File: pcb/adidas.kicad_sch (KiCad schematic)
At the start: 32 parts, among them J1 ISP Header, J7 Battery, J9 Shitty Add-on, U1 MPU-6050, U2 ATTINY841-SSU

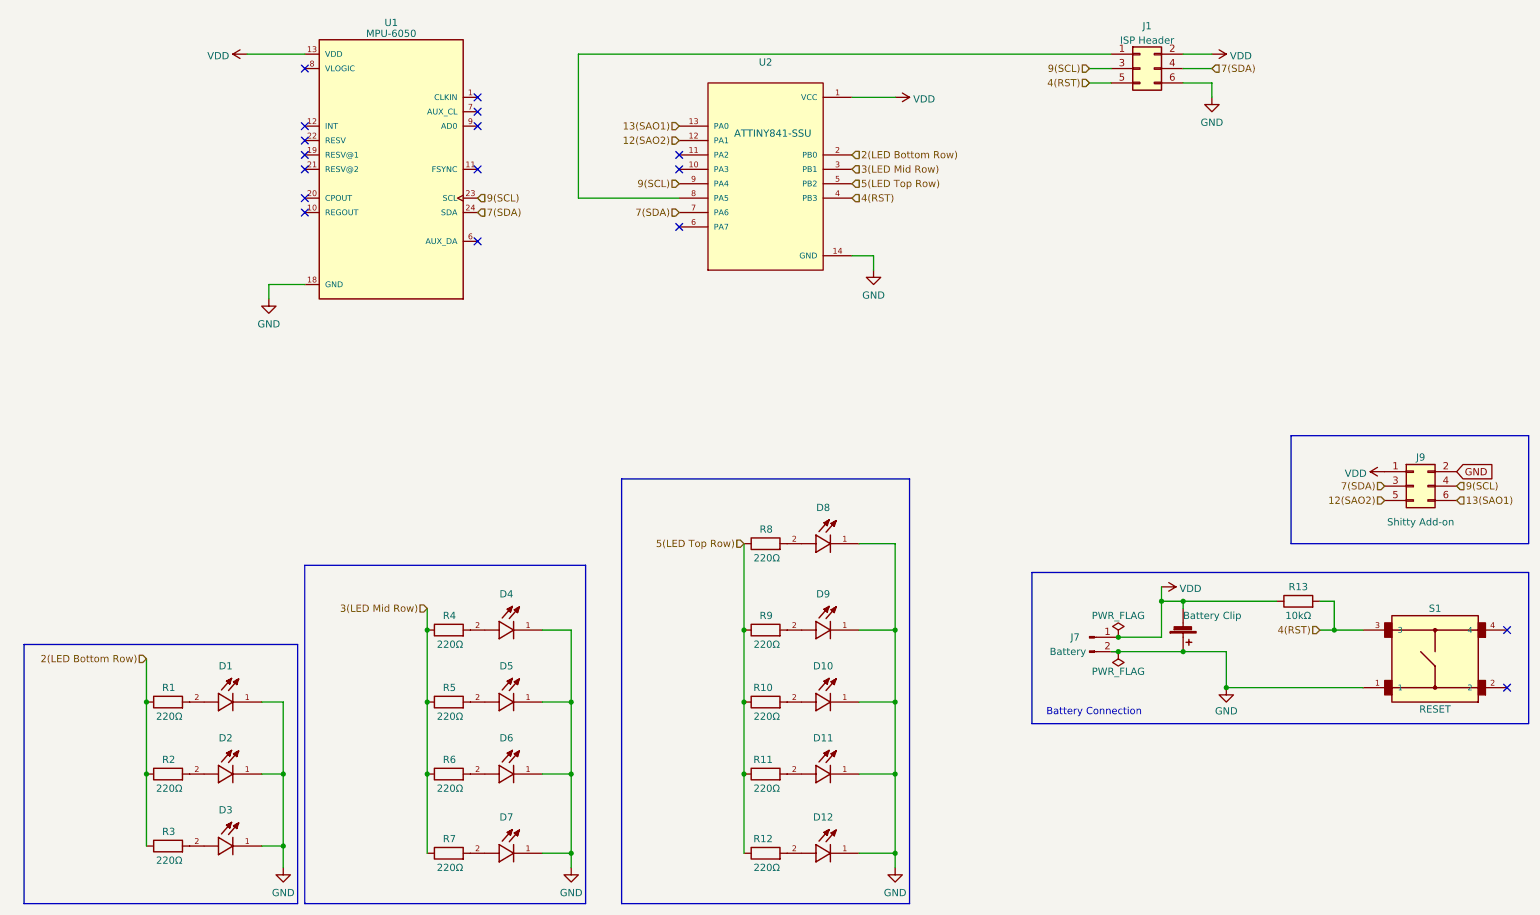
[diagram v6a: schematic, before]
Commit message: update switches, re-add the lanyard hole
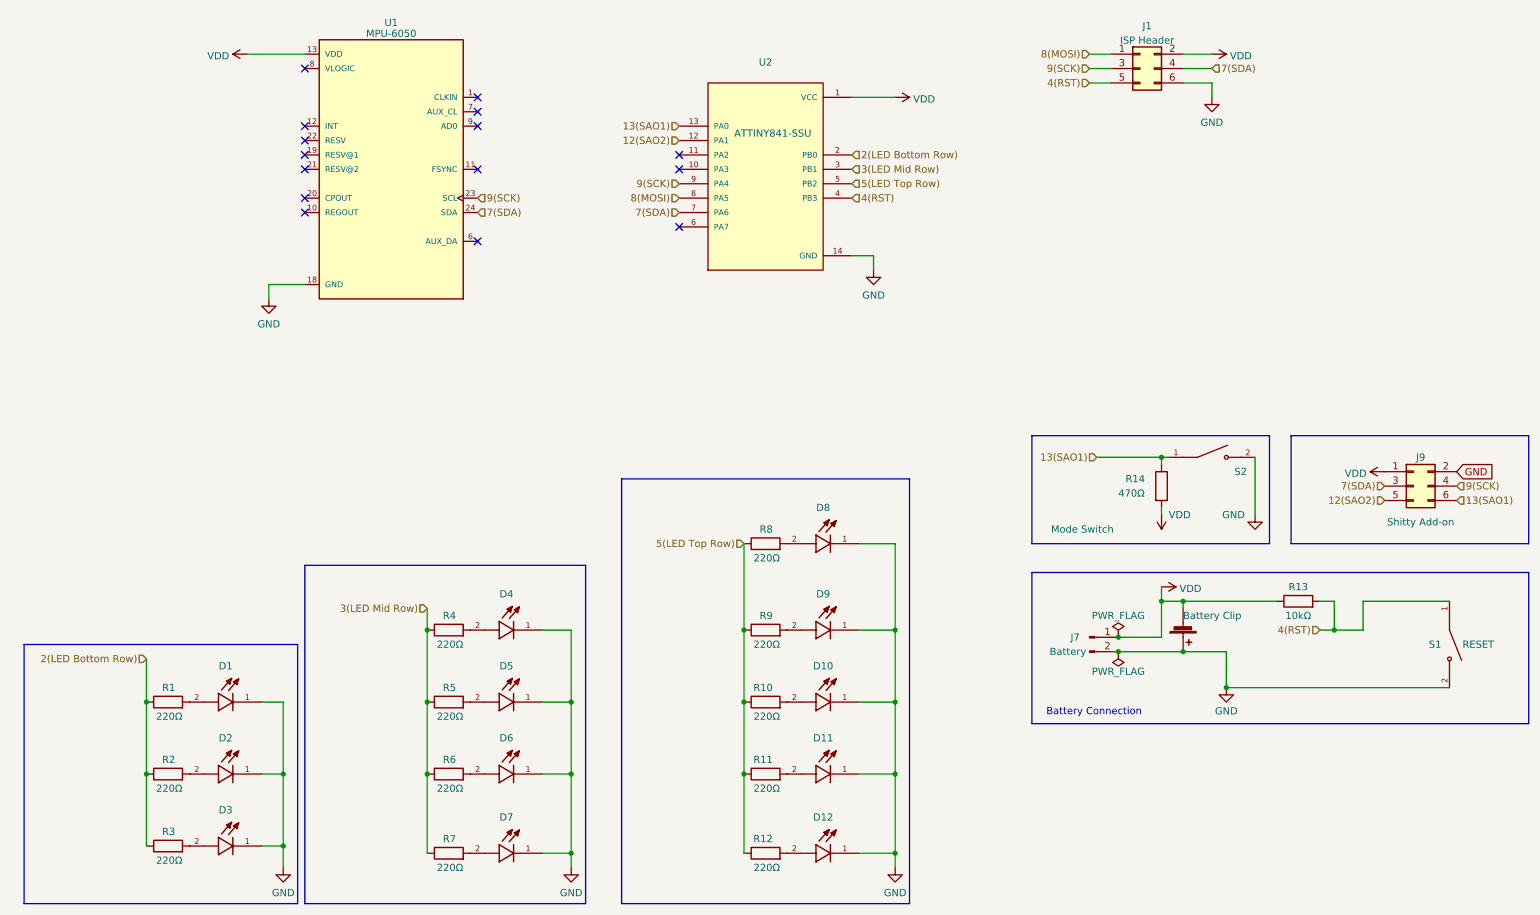
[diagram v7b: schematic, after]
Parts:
- added R14: 470Ω, Resistor_SMD:R_1206_3216Metric, symbol Device:R
- added S2: TL1107BF180WQ, DEAD10C5:SW_TL1107BF130WQ, symbol dead10c5:TL1107BF130WQ
- BT1: footprint DEAD10C5:BatteryHolder_Keystone_3002_1x2032 -> Resistor_SMD:R_1206_3216Metric
- S1: value B3F-1000 -> TL1107BF180WQ; footprint DEAD10C5:SW_B3F-1000 -> DEAD10C5:SW_TL1107BF130WQ; symbol dead10c5:B3F-1000 -> dead10c5:TL1107BF130WQ; Digi-Key Part Number SW400-ND -> EG2513-ND; MANUFACTURER (none) -> E-Switch; MAXIMUM_PACKAGE_HEIGHT (none) -> 4.3mm; Manufacturer Omron Electronics Inc-EMC Div -> E-Switch; SNAPEDA_PN (none) -> TL1107BF180WQ; now in the parts list
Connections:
- net 13(SAO1): now also R14.1, S2.1
- net 4(RST): now also S1.1; no longer S1.3
- net GND: now also S1.2, S2.2; no longer S1.1
- net VDD: now also R14.2
- net 8(MOSI): now reaches J1.1 (Pin_1), U2.8 (PA5)
- net 9(SCL) renamed 9(SCK)
- no-connect marks 17 -> 15
